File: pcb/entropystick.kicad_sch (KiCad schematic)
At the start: 25 parts, among them IC1 ICE40LP384-SG32, J1 USB_A, J2 TC2050, J3 Conn_02x04_Odd_Even, U1 CP2102-QFN28, U2 AT25DF256-XMHN-T, U3 MIC5365-1.2YC5, Y1 XO32

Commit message: improve pin assignments, place&route
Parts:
- removed J3: Conn_02x04_Odd_Even, Connector_PinHeader_2.54mm:PinHeader_2x04_P2.54mm_Vertical_SMD, symbol Connector_Generic:Conn_02x04_Odd_Even
- added J3: Conn_02x06_Odd_Even, Connector_PinHeader_1.27mm:PinHeader_2x06_P1.27mm_Vertical_SMD, symbol Connector_Generic:Conn_02x06_Odd_Even
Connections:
- net +3V3: now also J3.1 (Pin_1), J3.2 (Pin_2)
- net CLK32M: now also IC1.19 (19_GBIN); no longer IC1.20 (20_GBIN)
- net GND: now also J3.11 (Pin_11), J3.12 (Pin_12)
- net GPIO1: now also IC1.23, J3.3 (Pin_3); no longer IC1.22
- net GPIO2: now also IC1.30 (30_GBIN), J3.4 (Pin_4); no longer IC1.23
- net GPIO3: now also IC1.22, J3.5 (Pin_5); no longer IC1.26
- net GPIO4: now also IC1.29 (29_GBIN), J3.6 (Pin_6); no longer IC1.27
- net GPIO5: now also IC1.20 (20_GBIN), J3.7 (Pin_7); no longer IC1.29 (29_GBIN)
- net GPIO6: now also IC1.27, J3.8 (Pin_8); no longer IC1.30 (30_GBIN)
- net GPIO7: now also IC1.18, J3.9 (Pin_9); no longer IC1.31
- net GPIO8: now also IC1.26, J3.10 (Pin_10); no longer IC1.32
- net UART_CTS: now also IC1.8 (8_GBIN); no longer IC1.6 (6_GBIN)
- net UART_DCD: now also IC1.32; no longer IC1.18
- net UART_DSR: now also IC1.2; no longer IC1.7
- net UART_DTR: now also IC1.1; no longer IC1.8 (8_GBIN)
- net UART_RI: now also IC1.31; no longer IC1.19 (19_GBIN)
- net UART_RTS: now also IC1.7; no longer IC1.5
- net UART_RXD: now also IC1.6 (6_GBIN); no longer IC1.2
- net UART_TXD: now also IC1.5; no longer IC1.1

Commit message: improve PCB
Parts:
- added D2, D4: LED, LED_SMD:LED_0603_1608Metric, symbol Device:LED
- added R5, R6: 1k, Resistor_SMD:R_0603_1608Metric, symbol Device:R
- J3: footprint Connector_PinHeader_1.27mm:PinHeader_2x06_P1.27mm_Vertical_SMD -> Connector_PinHeader_2.54mm:PinHeader_2x06_P2.54mm_Vertical
- renumbered D2 to D3, R5 to R7
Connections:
- net +3V3: now also R5.1
- net GND: now also D2.1 (K), D4.1 (K)
- net SCK: now also R6.1
- new net: D4.2 (A), R6.2
- new net: D2.2 (A), R5.2
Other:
- moved on the sheet: C1, C2, C3, C4, R1, R4, U1

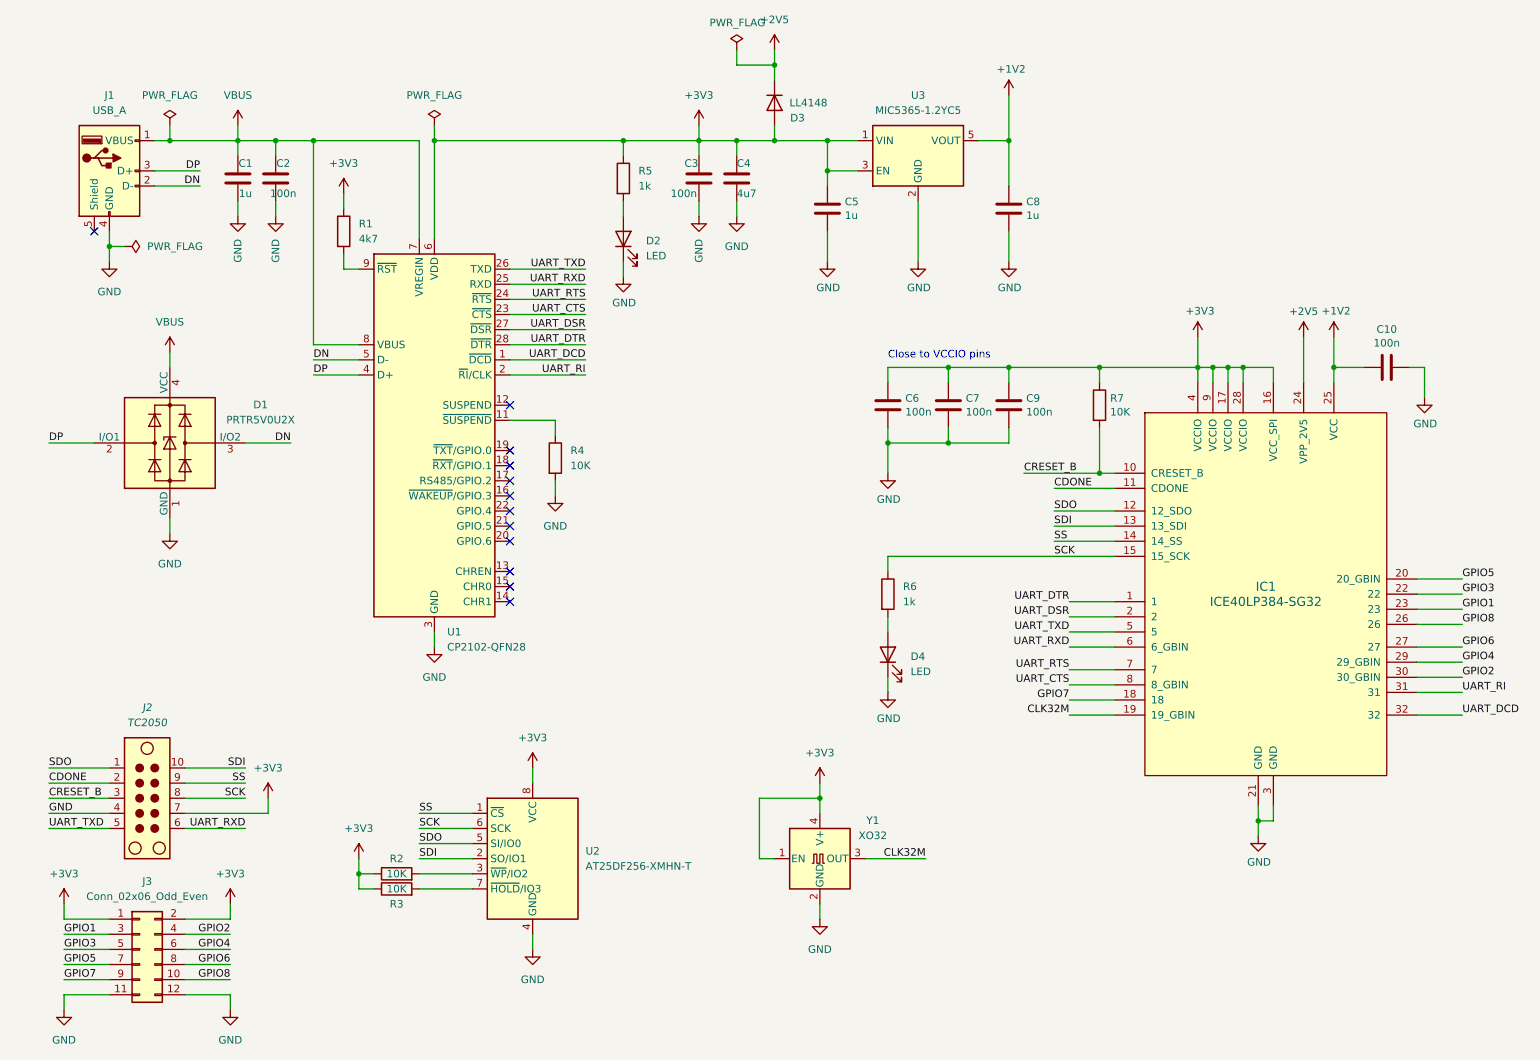
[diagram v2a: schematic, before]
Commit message: add switch, LED; verify USB connector dimensions
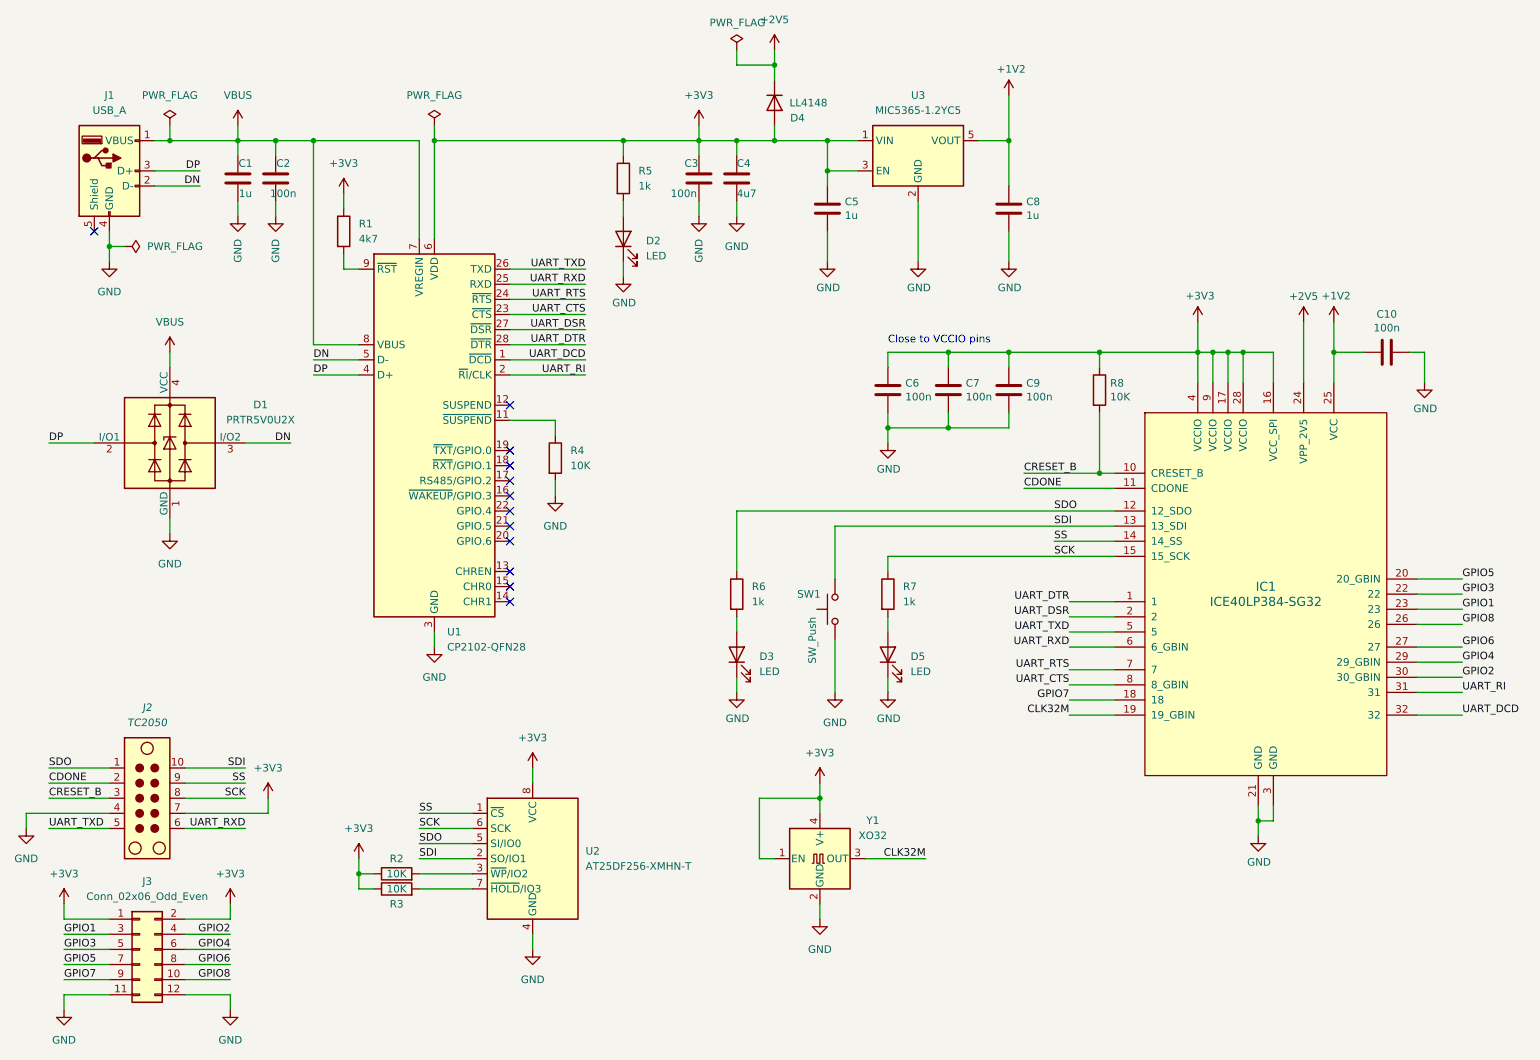
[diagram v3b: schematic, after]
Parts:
- added D3: LED, LED_SMD:LED_0603_1608Metric, symbol Device:LED
- added R6: 1k, Resistor_SMD:R_0603_1608Metric, symbol Device:R
- added SW1: SW_Push, dpiegdon:TS-1224W_Side_Button_2x4x3.3mm_3.5mm_3.8mm_SMD_Aliexpress, symbol Switch:SW_Push
- renumbered D3 to D4, D4 to D5, R6 to R7, R7 to R8
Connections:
- net GND: now also D3.1 (K), SW1.1
- net SDI: now also SW1.2
- net SDO: now also R6.1
- new net: D3.2 (A), R6.2
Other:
- moved on the sheet: C10, C6, C7, C9, R8
